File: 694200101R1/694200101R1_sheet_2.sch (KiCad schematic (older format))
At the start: 87 parts, among them U4 M24M02-DRMN6TP, U5 IS31FL3733B-QFLS4-TR, U6 IS31FL3733B-QFLS4-TR

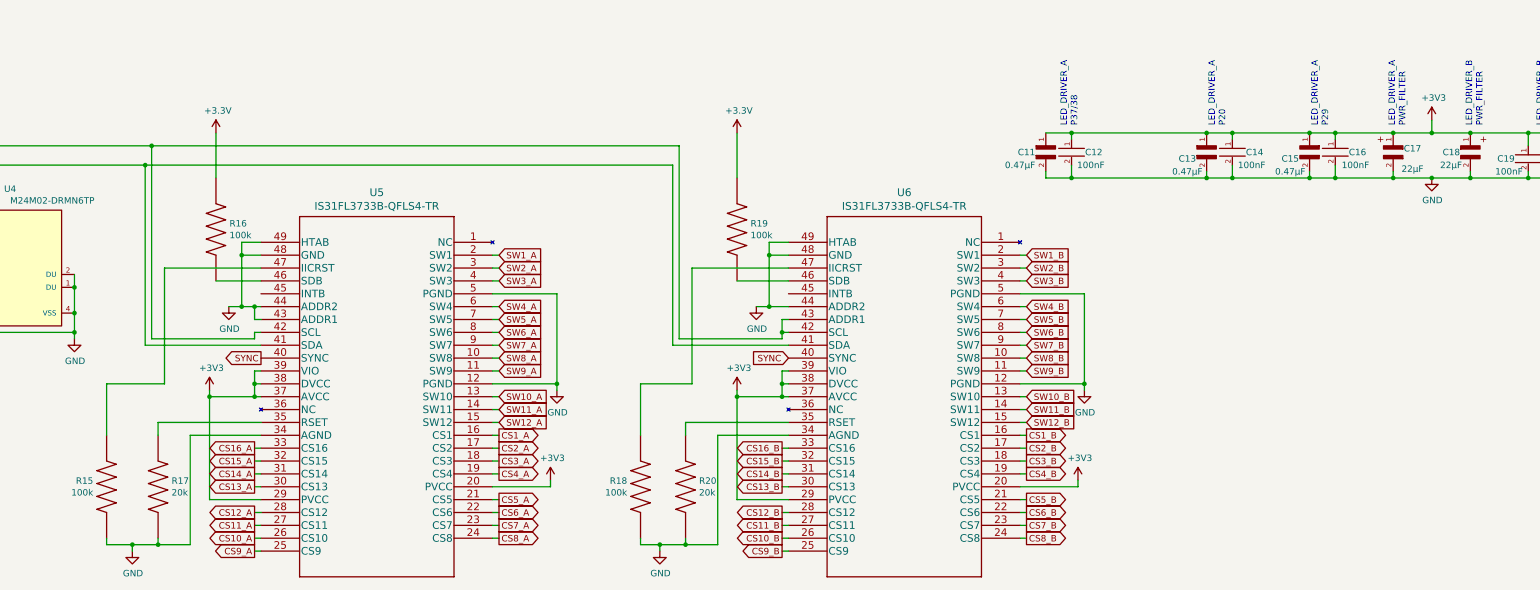
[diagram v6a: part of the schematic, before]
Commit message: fixed power to led drivers
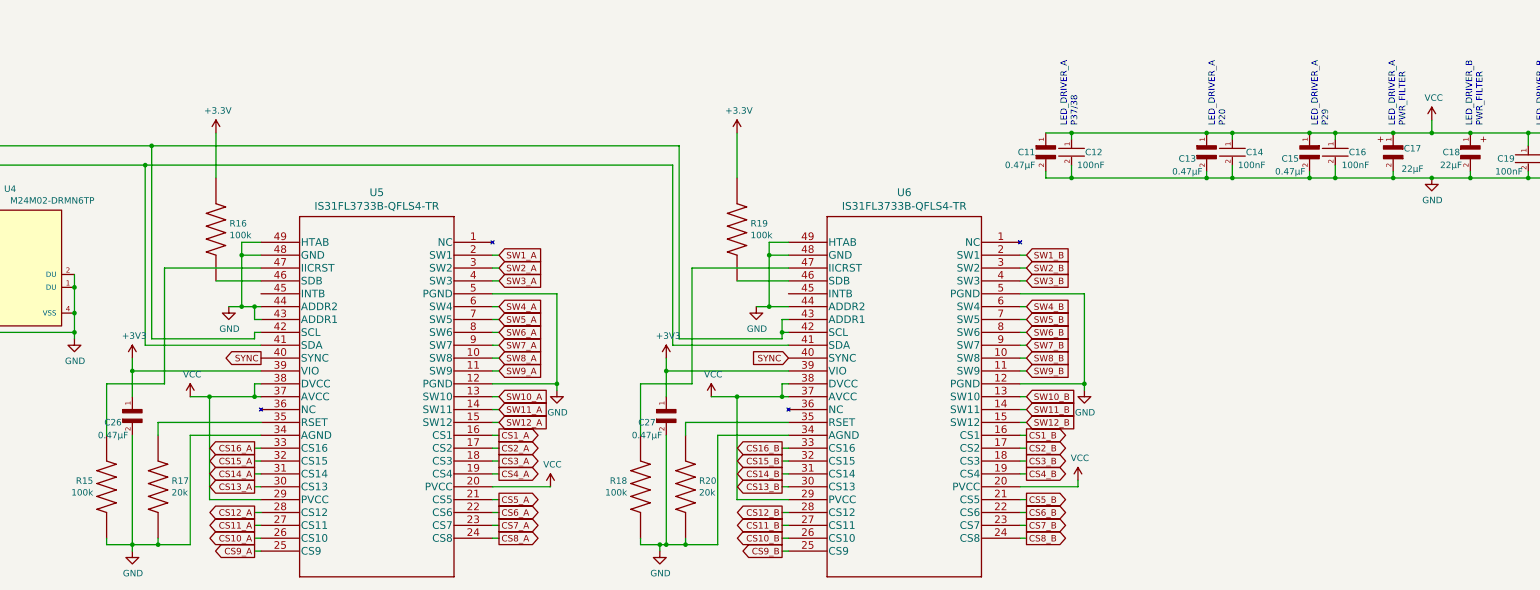
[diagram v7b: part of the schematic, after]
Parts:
- added C26, C27: CL10B474KA8NFNC, capacitor-lib:CAPC1608X90N, symbol capacitor-lib:CL10B474KA8NFNC
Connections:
- net +3V3: now also C26.1, C27.1; no longer C11.1, C12.1, C13.1, C14.1, C15.1, C16.1, C17.1, C18.1, C19.1, C20.1, C21.1, C22.1, C23.1, C24.1, U5.20 (PVCC), U5.29 (PVCC), U5.37 (AVCC), U5.38 (DVCC), U6.20 (PVCC), U6.29 (PVCC), U6.37 (AVCC), U6.38 (DVCC)
- net GND: now also C26.2, C27.2
- new net VCC: C11.1, C12.1, C13.1, C14.1, C15.1, C16.1, C17.1, C18.1, C19.1, C20.1, C21.1, C22.1, C23.1, C24.1, U5.20 (PVCC), U5.29 (PVCC), U5.37 (AVCC), U5.38 (DVCC), U6.20 (PVCC), U6.29 (PVCC), U6.37 (AVCC), U6.38 (DVCC)
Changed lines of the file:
@@
 Wire Wire Line
 	3950 8950 4000 8950
-Wire Wire Line
-	4000 8750 3950 8750
-Wire Wire Line
-	3950 8750 3950 8850
-Connection ~ 3950 8850
 Connection ~ 3950 8950
 Text Notes 10350 6850 1    50   ~ 0
@@
 Connection ~ 11350 7250
 Wire Wire Line
-	13100 6900 13100 6800
-Wire Wire Line
 	11550 7250 11550 7150
 Wire Wire Line
@@
 	3450 10100 3200 10100
 Wire Wire Line
-	3600 8900 3600 8950
-Wire Wire Line
 	3200 10050 3200 10100
 Connection ~ 3200 10100
@@
 	5800 9650 6250 9650
 Wire Wire Line
-	6250 9650 6250 9600
-Wire Wire Line
 	4000 7750 3850 7750
 Wire Wire Line
@@
 Wire Wire Line
 	3950 8950 3600 8950
-Wire Wire Line
-	3600 9750 3600 8950
 Text GLabel 3950 9550 0    50   Output ~ 0
 CS14_A
@@
 Wire Wire Line
 	8050 8950 8100 8950
-Wire Wire Line
-	8100 8750 8050 8750
-Wire Wire Line
-	8050 8750 8050 8850
-Connection ~ 8050 8850
 Connection ~ 8050 8950
 Connection ~ 7700 8950
@@
 	7550 10100 7300 10100
 Wire Wire Line
-	7700 8900 7700 8950
-Wire Wire Line
 	7300 10050 7300 10100
 Connection ~ 7300 10100
 Wire Wire Line
-	7300 10100 7100 10100
-Wire Wire Line
 	8100 9150 7300 9150
 Wire Wire Line
@@
 $EndComp
 $Comp
-L power:+3V3 #PWR029
-U 1 1 63D70980
-P 13100 6800
-F 0 "#PWR029" H 13100 6650 50  0001 C CNN
-F 1 "+3V3" H 13115 6973 50  0000 C CNN
-F 2 "" H 13100 6800 50  0001 C CNN
-F 3 "" H 13100 6800 50  0001 C CNN
-	1    13100 6800
-	1    0    0    -1
-$EndComp
-$Comp
 L capacitor-lib:CL10B474KA8NFNC C11
 U 1 1 63D72369
@@
 L power:+3V3 #PWR020
 U 1 1 63D94BE2
-P 3600 8900
-F 0 "#PWR020" H 3600 8750 50  0001 C CNN
-F 1 "+3V3" H 3615 9073 50  0000 C CNN
-F 2 "" H 3600 8900 50  0001 C CNN
-F 3 "" H 3600 8900 50  0001 C CNN
-	1    3600 8900
+P 3000 8650
+F 0 "#PWR020" H 3000 8500 50  0001 C CNN
+F 1 "+3V3" H 3015 8823 50  0000 C CNN
+F 2 "" H 3000 8650 50  0001 C CNN
+F 3 "" H 3000 8650 50  0001 C CNN
+	1    3000 8650
 	1    0    0    -1
 $EndComp
@@
 L power:+3V3 #PWR025
 U 1 1 6409AB1B
-P 7700 8900
-F 0 "#PWR025" H 7700 8750 50  0001 C CNN
-F 1 "+3V3" H 7715 9073 50  0000 C CNN
-F 2 "" H 7700 8900 50  0001 C CNN
-F 3 "" H 7700 8900 50  0001 C CNN
-	1    7700 8900
+P 7150 8650
+F 0 "#PWR025" H 7150 8500 50  0001 C CNN
+F 1 "+3V3" H 7165 8823 50  0000 C CNN
+F 2 "" H 7150 8650 50  0001 C CNN
+F 3 "" H 7150 8650 50  0001 C CNN
+	1    7150 8650
 	1    0    0    -1
 $EndComp
@@
 $EndComp
 $Comp
-L power:+3V3 #PWR027
-U 1 1 6409AB74
-P 10350 9600
-F 0 "#PWR027" H 10350 9450 50  0001 C CNN
-F 1 "+3V3" H 10365 9773 50  0000 C CNN
-F 2 "" H 10350 9600 50  0001 C CNN
-F 3 "" H 10350 9600 50  0001 C CNN
-	1    10350 9600
-	1    0    0    -1
-$EndComp
-$Comp
 L power:GND #PWR028
 U 1 1 6409AB6A
@@
 $EndComp
 $Comp
-L power:+3V3 #PWR022
-U 1 1 63F20B48
-P 6250 9600
-F 0 "#PWR022" H 6250 9450 50  0001 C CNN
-F 1 "+3V3" H 6265 9773 50  0000 C CNN
-F 2 "" H 6250 9600 50  0001 C CNN
-F 3 "" H 6250 9600 50  0001 C CNN
-	1    6250 9600
-	1    0    0    -1
-$EndComp
-$Comp
 L power:GND #PWR023
 U 1 1 63F0DD67
@@
 Connection ~ 12800 7250
 Connection ~ 13400 7250
-Wire Wire Line
-	13400 6900 13100 6900
 Connection ~ 13400 6900
-Wire Wire Line
-	12800 6900 13100 6900
 Connection ~ 12800 6900
-Connection ~ 13100 6900
 Connection ~ 13100 7250
 Wire Wire Line
@@
 Wire Wire Line
 	7700 7250 7700 6900
+Wire Wire Line
+	3600 8950 3450 8950
+Wire Wire Line
+	7700 8950 7500 8950
+$Comp
+L power:VCC #PWR?
+U 1 1 61D58879
+P 3450 8950
+AR Path="/61D58879" Ref="#PWR?"  Part="1"
+AR Path="/63A35802/61D58879" Ref="#PWR0113"  Part="1"
+F 0 "#PWR0113" H 3450 8800 50  0001 C CNN
+F 1 "VCC" H 3465 9123 50  0000 C CNN
+F 2 "" H 3450 8950 50  0001 C CNN
+F 3 "" H 3450 8950 50  0001 C CNN
+	1    3450 8950
+	1    0    0    -1
+$EndComp
+$Comp
+L power:VCC #PWR?
+U 1 1 61E34FF7
+P 6250 9650
+AR Path="/61E34FF7" Ref="#PWR?"  Part="1"
+AR Path="/63A35802/61E34FF7" Ref="#PWR0114"  Part="1"
+F 0 "#PWR0114" H 6250 9500 50  0001 C CNN
+F 1 "VCC" H 6265 9823 50  0000 C CNN
+F 2 "" H 6250 9650 50  0001 C CNN
+F 3 "" H 6250 9650 50  0001 C CNN
+	1    6250 9650
+	1    0    0    -1
+$EndComp
+$Comp
+L power:VCC #PWR?
+U 1 1 61FEDE4D
+P 10350 9600
+AR Path="/61FEDE4D" Ref="#PWR?"  Part="1"
+AR Path="/63A35802/61FEDE4D" Ref="#PWR0116"  Part="1"
+F 0 "#PWR0116" H 10350 9450 50  0001 C CNN
+F 1 "VCC" H 10365 9773 50  0000 C CNN
+F 2 "" H 10350 9600 50  0001 C CNN
+F 3 "" H 10350 9600 50  0001 C CNN
+	1    10350 9600
+	1    0    0    -1
+$EndComp
+$Comp
+L capacitor-lib:CL10B474KA8NFNC C26
+U 1 1 624BEE17
+P 3000 9050
+F 0 "C26" V 3100 8900 50  0000 C CNN
+F 1 "CL10B474KA8NFNC" H 3000 8850 50  0001 L BNN
+F 2 "capacitor-lib:CAPC1608X90N" H 3000 9050 50  0001 L BNN
+F 3 "" H 3000 9050 50  0001 L BNN
+F 4 "https://pricing.snapeda.com/search/part/CL10B474KA8NFNC/?ref=eda" H 3000 9050 50  0001 L BNN "Purchase-URL"
+F 5 "0603 Samsung" H 3000 9050 50  0001 L BNN "Package"
+F 6 "CL10B474KA8NFNC" H 3000 9050 50  0001 L BNN "MP"
+F 7 "1276-2082-1-ND" H 3000 9050 50  0001 L BNN "Digi-Key_Part_Number"
+F 8 "Samsung Electro-Mechanics" H 3000 9050 50  0001 L BNN "MF"
+F 9 "0.47µF ±10% 25V Ceramic Capacitor X7R 0603 (1608 Metric)" H 3000 9050 50  0001 L BNN "Description"
+F 10 "0.47µF" V 3200 8900 50  0000 C CNN "capacitance"
+	1    3000 9050
+	0    1    1    0
+$EndComp
+$Comp
+L capacitor-lib:CL10B474KA8NFNC C27
+U 1 1 6259BAD5
+P 7150 9050
+F 0 "C27" V 7250 8900 50  0000 C CNN
+F 1 "CL10B474KA8NFNC" H 7150 8850 50  0001 L BNN
+F 2 "capacitor-lib:CAPC1608X90N" H 7150 9050 50  0001 L BNN
+F 3 "" H 7150 9050 50  0001 L BNN
+F 4 "https://pricing.snapeda.com/search/part/CL10B474KA8NFNC/?ref=eda" H 7150 9050 50  0001 L BNN "Purchase-URL"
+F 5 "0603 Samsung" H 7150 9050 50  0001 L BNN "Package"
+F 6 "CL10B474KA8NFNC" H 7150 9050 50  0001 L BNN "MP"
+F 7 "1276-2082-1-ND" H 7150 9050 50  0001 L BNN "Digi-Key_Part_Number"
+F 8 "Samsung Electro-Mechanics" H 7150 9050 50  0001 L BNN "MF"
+F 9 "0.47µF ±10% 25V Ceramic Capacitor X7R 0603 (1608 Metric)" H 7150 9050 50  0001 L BNN "Description"
+F 10 "0.47µF" V 7350 8900 50  0000 C CNN "capacitance"
+	1    7150 9050
+	0    1    1    0
+$EndComp
+Wire Wire Line
+	3600 8950 3600 9750
+Wire Wire Line
+	3000 8650 3000 8750
+Wire Wire Line
+	3000 8750 4000 8750
+Connection ~ 3000 8750
+Wire Wire Line
+	3000 8750 3000 8950
+Wire Wire Line
+	3000 9250 3000 10100
+$Comp
+L power:VCC #PWR?
+U 1 1 61F1179C
+P 7500 8950
+AR Path="/61F1179C" Ref="#PWR?"  Part="1"
+AR Path="/63A35802/61F1179C" Ref="#PWR0115"  Part="1"
+F 0 "#PWR0115" H 7500 8800 50  0001 C CNN
+F 1 "VCC" H 7515 9123 50  0000 C CNN
+F 2 "" H 7500 8950 50  0001 C CNN
+F 3 "" H 7500 8950 50  0001 C CNN
+	1    7500 8950
+	1    0    0    -1
+$EndComp
+Wire Wire Line
+	7150 8650 7150 8750
+Wire Wire Line
+	7150 9250 7150 10100
+Wire Wire Line
+	7100 10100 7150 10100
+Connection ~ 7150 10100
+Wire Wire Line
+	7150 10100 7300 10100
+Wire Wire Line
+	7150 8750 8100 8750
+Connection ~ 7150 8750
+Wire Wire Line
+	7150 8750 7150 8950
+$Comp
+L power:VCC #PWR?
+U 1 1 6364BAD2
+P 13100 6800
+AR Path="/6364BAD2" Ref="#PWR?"  Part="1"
+AR Path="/63A35802/6364BAD2" Ref="#PWR?"  Part="1"
+F 0 "#PWR?" H 13100 6650 50  0001 C CNN
+F 1 "VCC" H 13115 6973 50  0000 C CNN
+F 2 "" H 13100 6800 50  0001 C CNN
+F 3 "" H 13100 6800 50  0001 C CNN
+	1    13100 6800
+	1    0    0    -1
+$EndComp
+Wire Wire Line
+	12800 6900 13100 6900
+Wire Wire Line
+	13400 6900 13100 6900
+Connection ~ 13100 6900
+Wire Wire Line
+	13100 6900 13100 6800
 $EndSCHEMATC

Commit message: new resistor
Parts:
- R17, R20: value RMCF2512FT20K0 -> RMCF2512FT59K0; resistance 20k -> 59k
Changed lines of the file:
@@
 P 3200 9650
 F 0 "R17" V 3154 9755 50  0000 L CNN
-F 1 "RMCF2512FT20K0" H 2900 9450 50  0001 L BNN
+F 1 "RMCF2512FT59K0" H 2900 9450 50  0001 L BNN
 F 2 "Resistor-Libs:RESC6332X70N" H 3200 9650 50  0001 L BNN
 F 3 "" H 3200 9650 50  0001 L BNN
-F 4 "20k" V 3245 9755 50  0000 L CNN "resistance"
+F 4 "59k" V 3245 9755 50  0000 L CNN "resistance"
 	1    3200 9650
 	0    1    1    0
@@
 P 7300 9650
 F 0 "R20" V 7254 9755 50  0000 L CNN
-F 1 "RMCF2512FT20K0" H 7000 9450 50  0001 L BNN
+F 1 "RMCF2512FT59K0" H 7000 9450 50  0001 L BNN
 F 2 "Resistor-Libs:RESC6332X70N" H 7300 9650 50  0001 L BNN
 F 3 "" H 7300 9650 50  0001 L BNN
-F 4 "20k" V 7345 9755 50  0000 L CNN "resistance"
+F 4 "59k" V 7345 9755 50  0000 L CNN "resistance"
 	1    7300 9650
 	0    1    1    0
